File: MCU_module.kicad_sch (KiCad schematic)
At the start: 7 parts, among them U1 STM32C011F4U6TR, Y1 Crystal

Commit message: First basic design
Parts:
- removed C3, C4: CL, symbol Device:C_Small
- removed R1: R_Ref, symbol Device:R_Small
- removed U1: STM32C011F4U6TR, Package_DFN_QFN:ST_UFQFPN-20_3x3mm_P0.5mm, symbol MCU_ST_STM32C0:STM32C011F_4-6_Ux
- removed Y1: Crystal, symbol Device:Crystal_GND24
- added BOOT0: SW2, symbol Switch:SW_SPDT
- added C13: 4.7u, Capacitor_SMD:C_0402_1005Metric, symbol Device:C_Small
- added C14: 100n, Capacitor_SMD:C_0402_1005Metric, symbol Device:C_Small
- added C15: 1u, Capacitor_SMD:C_0402_1005Metric, symbol Device:C_Small
- added C16: 10n, Capacitor_SMD:C_0402_1005Metric, symbol Device:C_Small
- added C21: 0.1u, Capacitor_SMD:C_0402_1005Metric, symbol Device:C_Small
- added J2: SWD, Connector_PinHeader_1.27mm:PinHeader_2x05_P1.27mm_Vertical_SMD, symbol Connector_Generic:Conn_02x05_Odd_Even
- added R4: 10k, Resistor_SMD:R_0603_1608Metric, symbol Device:R_Small
- added SW1: NRST, symbol Switch:SW_SPST
- added U1: STM32F042G6U6, Package_DFN_QFN:QFN-28_4x4mm_P0.5mm, symbol MCU_ST_STM32F0:STM32F042G6Ux
- C1, C2: footprint (none) -> Capacitor_SMD:C_0402_1005Metric
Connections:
- net +3V3: now also BOOT0.3 (C), C13.1, C14.1, C15.1, C16.1, J2.1 (Pin_1), U1.17 (VDD), U1.18 (VDDIO2), U1.5 (VDDA)
- net GND: now also BOOT0.1 (A), C13.2, C14.2, C15.2, C16.2, C21.1, J2.3 (Pin_3), J2.5 (Pin_5), J2.9 (Pin_9), SW1.1 (A), U1.16 (VSSA)
- net SPI_CS: now also U1.23 (PA15)
- net SPI_MISO: now also U1.25 (PB4)
- net SPI_MOSI: now also U1.26 (PB5)
- net SPI_SCK: now also U1.24 (PB3)
- new net: BOOT0.2 (B), R4.1
- new net: R4.2, U1.1 (PB8)
- new net NRST: C21.2, J2.10 (Pin_10), SW1.2 (B), U1.4 (NRST)
- new net RF_CE: U1.27 (PB6)
- new net RF_IRQ: U1.28 (PB7)
- new net SWCLK: J2.4 (Pin_4), U1.22 (PA14)
- new net SWDIO: J2.2 (Pin_2), U1.21 (PA13)
- new net USB_D+: U1.20 (PA10/PA12)
- new net USB_D-: U1.19 (PA9/PA11)
- no-connect marks 0 -> 3

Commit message: Easier BOOT0
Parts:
- removed BOOT0: SW2, symbol Switch:SW_SPDT
- removed SW1: NRST, symbol Switch:SW_SPST
- added SW1: NRST, Button_Switch_SMD:SW_SPST_B3S-1000, symbol Switch:SW_Push
- added SW2: BOOT0, Button_Switch_SMD:SW_SPST_B3S-1000, symbol Switch:SW_Push
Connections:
- net +3V3: now also SW2.2
- net GND: now also R4.1, SW1.1
- net NRST: now also SW1.2
- net at R4.2, U1.1 (PB8): now also SW2.1
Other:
- moved on the sheet: R4

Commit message: Redesigned power supply. First board draft
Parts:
- SW1, SW2: footprint Button_Switch_SMD:SW_SPST_B3S-1000 -> Button_Switch_SMD:SW_SPST_B3U-1000P; JLCPCB C2733655 -> C231329
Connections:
- no-connect marks 3 -> 15
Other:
- moved on the sheet: C1, C13, C14, C15, C16, C2

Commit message: BOM assigned
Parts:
- C1, C13: LCSC (none) -> C82453
- C14, C2: LCSC (none) -> C1525
- C15: LCSC (none) -> C52923
- C16: LCSC (none) -> C15195
- C21: value 0.1u -> 100n; LCSC (none) -> C1525
- J2: LCSC (none) -> C4943297
- R4: LCSC (none) -> C25804
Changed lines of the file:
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@@
+			)
+		)
+		(property "LCSC" "C1525"
+			(at 181.61 31.75 0)
+			(effects
+				(font
+					(size 1.27 1.27)
+				)
+				(hide yes)
 			)
 		)
@@
 			)
 		)
+		(property "LCSC" "C4943297"
+			(at 113.03 43.18 0)
+			(effects
+				(font
+					(size 1.27 1.27)
+				)
+				(hide yes)
+			)
+		)
 		(pin "9"
 		)
@@
 			)
 		)
+		(property "LCSC" "C82453"
+			(at 172.72 31.75 0)
+			(effects
+				(font
+					(size 1.27 1.27)
+				)
+				(hide yes)
+			)
+		)
 		(pin "2"
 		)
@@
 			)
 		)
-		(property "Value" "0.1u"
+		(property "Value" "100n"
 			(at 156.2163 62.23 90)
 			(effects
@@
 			)
 		)
+		(property "LCSC" "C1525"
+			(at 156.21 66.04 90)
+			(effects
+				(font
+					(size 1.27 1.27)
+				)
+				(hide yes)
+			)
+		)
 		(pin "1"
 		)
@@
 			)
 		)
+		(property "LCSC" "C1525"
+			(at 163.83 31.75 0)
+			(effects
+				(font
+					(size 1.27 1.27)
+				)
+				(hide yes)
+			)
+		)
 		(pin "2"
 		)
@@
 			)
 		)
+		(property "LCSC" "C15195"
+			(at 199.39 31.75 0)
+			(effects
+				(font
+					(size 1.27 1.27)
+				)
+				(hide yes)
+			)
+		)
 		(pin "2"
 		)
@@
 			)
 		)
+		(property "LCSC" "C25804"
+			(at 142.24 109.22 0)
+			(effects
+				(font
+					(size 1.27 1.27)
+				)
+				(hide yes)
+			)
+		)
 		(pin "2"
 		)
@@
 			)
 		)
+		(property "LCSC" "C82453"
+			(at 154.94 31.75 0)
+			(effects
+				(font
+					(size 1.27 1.27)
+				)
+				(hide yes)
+			)
+		)
 		(pin "2"
 		)
@@
 			(at 190.5 31.75 0)
 			(effects
+				(font
+					(size 1.27 1.27)
+				)
+				(hide yes)
+			)
+		)
+		(property "LCSC" "C52923"
+			(at 190.5 31.75 0)
+			(effects

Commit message: Minor changes
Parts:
- C1, C13: LCSC C82453 -> (none); MPN (none) -> C82453
- C14, C2, C21: LCSC C1525 -> (none); MPN (none) -> C1525
- C15: LCSC C52923 -> (none); MPN (none) -> C52923
- C16: LCSC C15195 -> (none); MPN (none) -> C15195
- J2: footprint Connector_PinHeader_1.27mm:PinHeader_2x05_P1.27mm_Vertical_SMD -> Custom_Connectors:PinHeader_2x05_P1.27mm_Vertical_SMD_w_fiducials; JLCPCB Rotation Offset (none) -> -90; LCSC C4943297 -> (none); MPN (none) -> C4943297
- R4: LCSC C25804 -> (none); MPN (none) -> C25804
- SW1, SW2: JLCPCB C231329 -> (none); MPN (none) -> C231329
- U1: JLCPCB Rotation Offset (none) -> -90; LCSC C961597 -> (none); MPN (none) -> C961597
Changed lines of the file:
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@@
 			)
 		)
-		(property "LCSC" "C1525"
+		(property "MPN" "C1525"
 			(at 181.61 31.75 0)
 			(effects
@@
 			)
 		)
-		(property "Footprint" "Connector_PinHeader_1.27mm:PinHeader_2x05_P1.27mm_Vertical_SMD"
+		(property "Footprint" "Custom_Connectors:PinHeader_2x05_P1.27mm_Vertical_SMD_w_fiducials"
 			(at 113.03 43.18 0)
 			(effects
@@
 			)
 		)
-		(property "LCSC" "C4943297"
+		(property "MPN" "C4943297"
+			(at 113.03 43.18 0)
+			(effects
+				(font
+					(size 1.27 1.27)
+				)
+				(hide yes)
+			)
+		)
+		(property "JLCPCB Rotation Offset" "-90"
 			(at 113.03 43.18 0)
 			(effects
@@
 			)
 		)
-		(property "LCSC" "C82453"
+		(property "MPN" "C82453"
 			(at 172.72 31.75 0)
 			(effects
@@
 			)
 		)
-		(property "JLCPCB" "C231329"
+		(property "MPN" "C231329"
 			(at 156.21 55.88 0)
 			(effects
@@
 			)
 		)
-		(property "JLCPCB" "C231329"
+		(property "MPN" "C231329"
 			(at 142.24 97.79 0)
 			(effects
@@
 			)
 		)
-		(property "LCSC" "C961597"
+		(property "MPN" "C961597"
+			(at 186.69 91.44 0)
+			(effects
+				(font
+					(size 1.27 1.27)
+				)
+				(hide yes)
+			)
+		)
+		(property "JLCPCB Rotation Offset" "-90"
 			(at 186.69 91.44 0)
 			(effects
@@
 			)
 		)
-		(property "LCSC" "C1525"
+		(property "MPN" "C1525"
 			(at 156.21 66.04 90)
 			(effects
@@
 			)
 		)
-		(property "LCSC" "C1525"
+		(property "MPN" "C1525"
 			(at 163.83 31.75 0)
 			(effects
@@
 			)
 		)
-		(property "LCSC" "C15195"
+		(property "MPN" "C15195"
 			(at 199.39 31.75 0)
 			(effects
@@
 			)
 		)
-		(property "LCSC" "C25804"
+		(property "MPN" "C25804"
 			(at 142.24 109.22 0)
 			(effects
@@
 			)
 		)
-		(property "LCSC" "C82453"
+		(property "MPN" "C82453"
 			(at 154.94 31.75 0)
 			(effects
@@
 			)
 		)
-		(property "LCSC" "C52923"
+		(property "MPN" "C52923"
 			(at 190.5 31.75 0)
 			(effects

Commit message: Larger dimensions. Include mounting holes. Better antenna feed alignment
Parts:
- R4: footprint Resistor_SMD:R_0603_1608Metric -> Resistor_SMD:R_0402_1005Metric; MPN C25804 -> C25744
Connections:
- net GND: now also C21.2; no longer C21.1
- net NRST: now also C21.1; no longer C21.2
- net RF_CE: now also U1.8 (PA2); no longer U1.27 (PB6)
- net RF_IRQ: now also U1.2 (PF0); no longer U1.28 (PB7)
- net boot0: now reaches R4.2, SW2.1, U1.1 (PB8)
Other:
- moved on the sheet: C21
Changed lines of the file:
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@@
+	)
+	(no_connect
+		(at 171.45 99.06)
 	)
 	(no_connect
@@
 	)
 	(no_connect
-		(at 171.45 78.74)
+		(at 204.47 88.9)
 	)
 	(no_connect
-		(at 204.47 88.9)
-	)
-	(no_connect
-		(at 204.47 78.74)
+		(at 171.45 101.6)
 	)
 	(no_connect
@@
 	(wire
 		(pts
-			(xy 158.75 93.98) (xy 158.75 85.09)
+			(xy 148.59 93.98) (xy 148.59 85.09)
 		)
 		(stroke
@@
 	(wire
 		(pts
-			(xy 171.45 96.52) (xy 156.21 96.52)
+			(xy 171.45 96.52) (xy 146.05 96.52)
 		)
 		(stroke
@@
 	(wire
 		(pts
-			(xy 151.13 101.6) (xy 151.13 85.09)
-		)
-		(stroke
-			(width 0)
-			(type default)
-		)
-	)
-	(wire
-		(pts
 			(xy 163.83 34.29) (xy 163.83 36.83)
 		)
@@
 	(wire
 		(pts
-			(xy 171.45 101.6) (xy 151.13 101.6)
-		)
-		(stroke
-			(width 0)
-			(type default)
-		)
-	)
-	(wire
-		(pts
 			(xy 96.52 43.18) (xy 96.52 48.26)
 		)
@@
 	(wire
 		(pts
-			(xy 171.45 93.98) (xy 158.75 93.98)
+			(xy 171.45 93.98) (xy 148.59 93.98)
 		)
 		(stroke
@@
 	(wire
 		(pts
-			(xy 153.67 99.06) (xy 153.67 85.09)
-		)
-		(stroke
-			(width 0)
-			(type default)
-		)
-	)
-	(wire
-		(pts
 			(xy 163.83 36.83) (xy 154.94 36.83)
 		)
@@
 	(wire
 		(pts
-			(xy 156.21 96.52) (xy 156.21 85.09)
-		)
-		(stroke
-			(width 0)
-			(type default)
-		)
-	)
-	(wire
-		(pts
-			(xy 171.45 99.06) (xy 153.67 99.06)
+			(xy 146.05 96.52) (xy 146.05 85.09)
+		)
+		(stroke
+			(width 0)
+			(type default)
+		)
+	)
+	(wire
+		(pts
+			(xy 212.09 78.74) (xy 212.09 76.2)
 		)
 		(stroke
@@
 	(wire
 		(pts
-			(xy 161.29 91.44) (xy 161.29 85.09)
+			(xy 151.13 91.44) (xy 151.13 85.09)
 		)
 		(stroke
@@
 	(wire
 		(pts
+			(xy 165.1 78.74) (xy 171.45 78.74)
+		)
+		(stroke
+			(width 0)
+			(type default)
+		)
+	)
+	(wire
+		(pts
 			(xy 154.94 34.29) (xy 154.94 36.83)
 		)
@@
 	(wire
 		(pts
+			(xy 204.47 78.74) (xy 212.09 78.74)
+		)
+		(stroke
+			(width 0)
+			(type default)
+		)
+	)
+	(wire
+		(pts
 			(xy 171.45 73.66) (xy 163.83 73.66)
 		)
@@
 	(wire
 		(pts
-			(xy 171.45 91.44) (xy 161.29 91.44)
+			(xy 171.45 91.44) (xy 151.13 91.44)
 		)
 		(stroke
@@
 		)
 	)
-	(label "SWCLK"
-		(at 120.65 40.64 0)
+	(label "boot0"
+		(at 149.86 104.14 0)
 		(fields_autoplaced yes)
 		(effects
@@
 		)
 	)
-	(label "NRST"
-		(at 120.65 48.26 0)
+	(label "SWCLK"
+		(at 120.65 40.64 0)
 		(fields_autoplaced yes)
 		(effects
@@
 		)
 	)
-	(label "SWDIO"
-		(at 214.63 99.06 0)
+	(label "NRST"
+		(at 120.65 48.26 0)
 		(fields_autoplaced yes)
 		(effects
@@
 	)
 	(label "SWDIO"
-		(at 120.65 38.1 0)
+		(at 214.63 99.06 0)
 		(fields_autoplaced yes)
 		(effects
@@
 		)
 	)
-	(label "NRST"
-		(at 165.1 73.66 0)
+	(label "SWDIO"
+		(at 120.65 38.1 0)
 		(fields_autoplaced yes)
 		(effects
@@
 		)
 	)
-	(hierarchical_label "SPI_MOSI"
-		(shape input)
-		(at 156.21 85.09 90)
+	(label "NRST"
+		(at 165.1 73.66 0)
 		(fields_autoplaced yes)
 		(effects
@@
 				(size 1.27 1.27)
 			)
+			(justify left bottom)
+		)
+	)
+	(hierarchical_label "SPI_MOSI"
+		(shape input)
+		(at 146.05 85.09 90)
+		(fields_autoplaced yes)
+		(effects
+			(font
+				(size 1.27 1.27)
+			)
 			(justify left)
 		)
@@
 	(hierarchical_label "SPI_SCK"
 		(shape input)
-		(at 161.29 85.09 90)
+		(at 151.13 85.09 90)
 		(fields_autoplaced yes)
 		(effects
@@
 	(hierarchical_label "SPI_MISO"
 		(shape input)
-		(at 158.75 85.09 90)
+		(at 148.59 85.09 90)
 		(fields_autoplaced yes)
 		(effects
@@
 	(hierarchical_label "RF_IRQ"
 		(shape input)
-		(at 151.13 85.09 90)
+		(at 165.1 78.74 180)
 		(fields_autoplaced yes)
 		(effects
@@
 				(size 1.27 1.27)
 			)
-			(justify left)
+			(justify right)
 		)
 	)
 	(hierarchical_label "RF_CE"
 		(shape input)
-		(at 153.67 85.09 90)
+		(at 212.09 76.2 90)
 		(fields_autoplaced yes)
 		(effects
@@
 	(symbol
 		(lib_id "Device:C_Small")
-		(at 156.21 66.04 90)
+		(at 156.21 66.04 270)
+		(mirror x)
 		(unit 1)
 		(exclude_from_sim no)
@@
 		(on_board yes)
 		(dnp no)
-		(fields_autoplaced yes)
 		(property "Reference" "C21"
-			(at 156.2163 59.69 90)
+			(at 156.2037 59.69 90)
 			(effects
 				(font
@@
 		)
 		(property "Value" "100n"
-			(at 156.2163 62.23 90)
+			(at 156.2037 62.23 90)
 			(effects
 				(font
@@
 			)
 		)
-		(property "Footprint" "Resistor_SMD:R_0603_1608Metric"
+		(property "Footprint" "Resistor_SMD:R_0402_1005Metric"
 			(at 142.24 109.22 0)
 			(effects
@@
 			)
 		)
-		(property "MPN" "C25804"
+		(property "MPN" "C25744"
 			(at 142.24 109.22 0)
 			(effects

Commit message: Add signaling LEDs
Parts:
- added D301: SIG1, LED_SMD:LED_0603_1608Metric, symbol Device:LED_Small
- added D302: SIG2, LED_SMD:LED_0603_1608Metric, symbol Device:LED_Small
- added D303: SIG3, LED_SMD:LED_0603_1608Metric, symbol Device:LED_Small
- added D304: SIG4, LED_SMD:LED_0603_1608Metric, symbol Device:LED_Small
- added R301, R302, R303, R304: 2k2, Resistor_SMD:R_0402_1005Metric, symbol Device:R_Small
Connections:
- net GND: now also R301.2, R302.2, R303.2, R304.2
- net SIG3: now reaches U1.10 (PA4)
- net SIG3: now also D303.2 (A)
- net SIG2: now reaches U1.11 (PA5)
- net SIG2: now also D302.2 (A)
- net SIG1: now reaches U1.12 (PA6)
- net SIG1: now also D301.2 (A)
- net SIG4: now reaches U1.9 (PA3)
- net SIG4: now also D304.2 (A)
- new net: D304.1 (K), R304.1
- new net: D303.1 (K), R303.1
- new net: D301.1 (K), R301.1
- new net: D302.1 (K), R302.1
- no-connect marks 15 -> 11

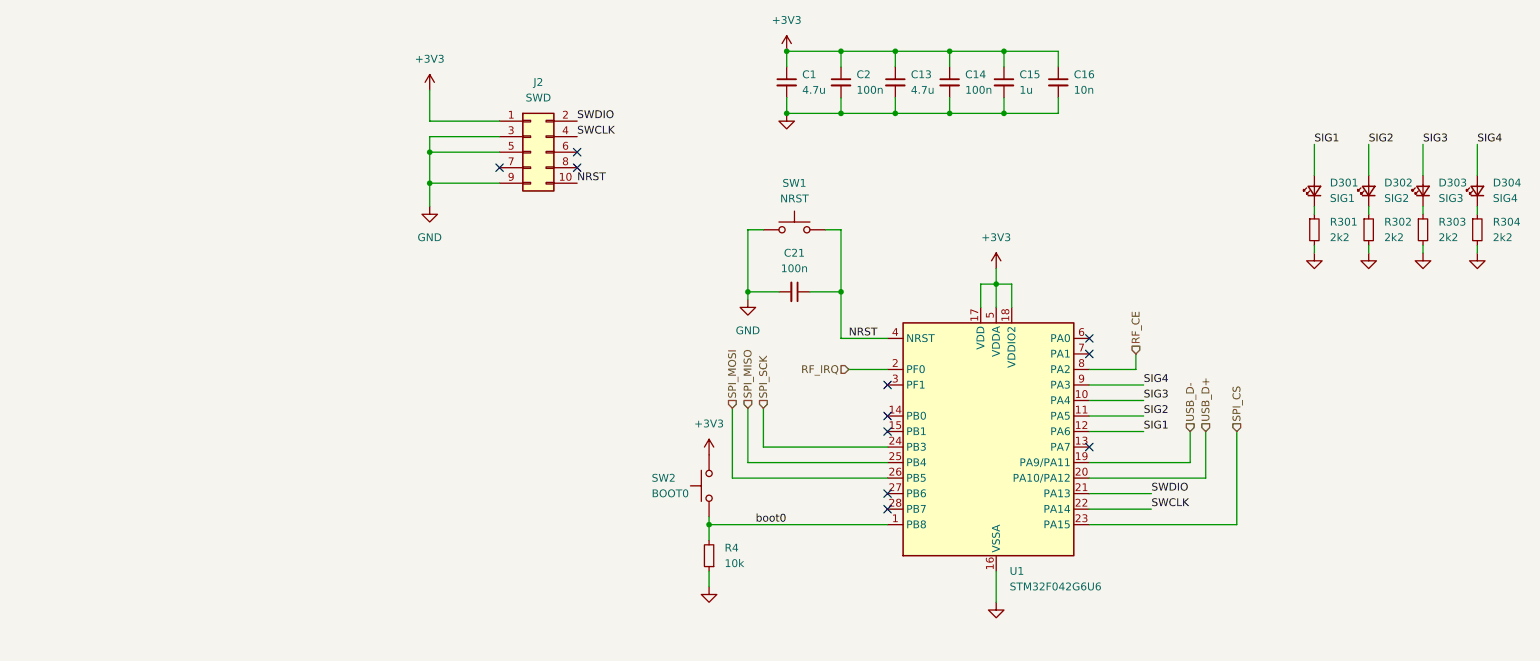
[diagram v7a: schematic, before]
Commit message: Migrated the STM32F0 to an STM32G0B
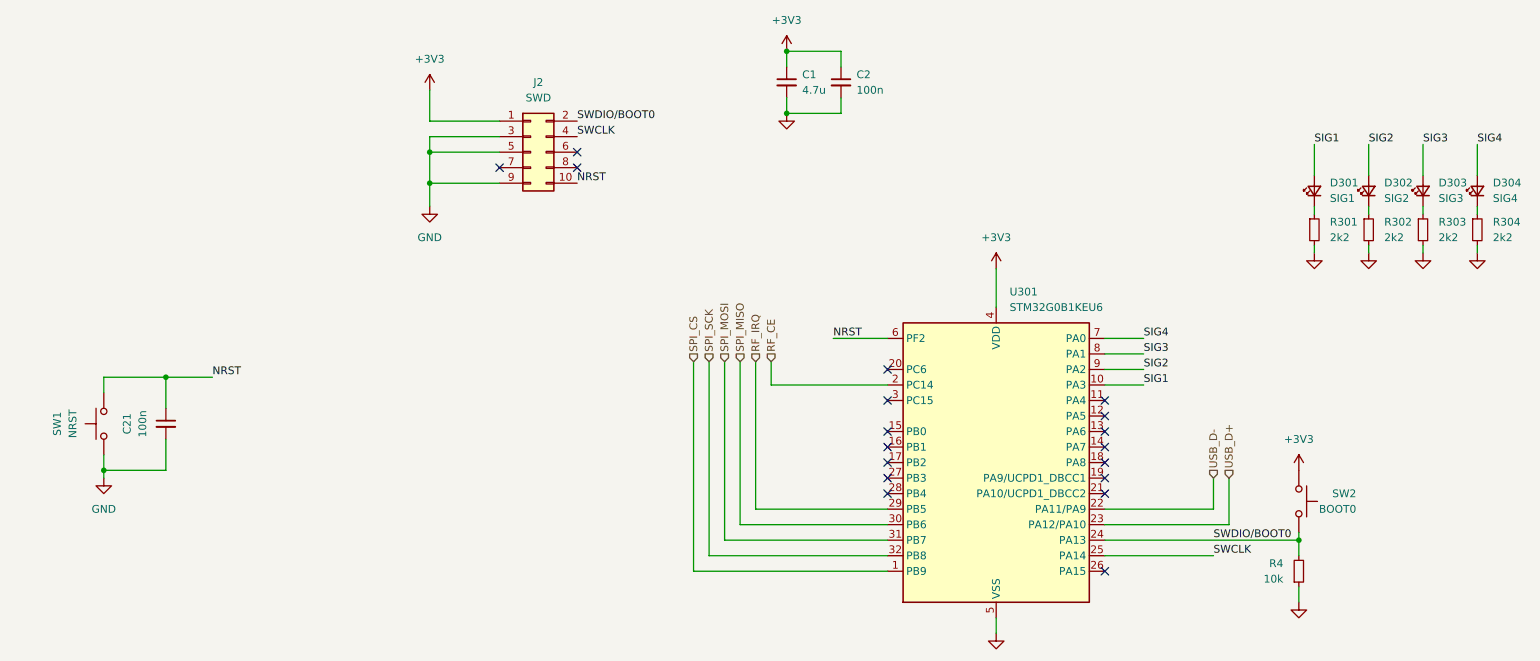
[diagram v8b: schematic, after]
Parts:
- removed C13: 4.7u, Capacitor_SMD:C_0402_1005Metric, symbol Device:C_Small
- removed C14: 100n, Capacitor_SMD:C_0402_1005Metric, symbol Device:C_Small
- removed C15: 1u, Capacitor_SMD:C_0402_1005Metric, symbol Device:C_Small
- removed C16: 10n, Capacitor_SMD:C_0402_1005Metric, symbol Device:C_Small
- removed U1: STM32F042G6U6, Package_DFN_QFN:QFN-28_4x4mm_P0.5mm, symbol MCU_ST_STM32F0:STM32F042G6Ux
- added U301: STM32G0B1KEU6, Package_DFN_QFN:QFN-32-1EP_5x5mm_P0.5mm_EP3.45x3.45mm, symbol MCU_ST_STM32G0:STM32G0B1KEUx
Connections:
- net boot0 is gone; now on net SWDIO/BOOT0: R4.2, SW2.1
- net +3V3: now also U301.4 (VDD)
- net GND: now also U301.33 (VSS), U301.5 (VSS)
- net NRST: now also U301.6 (PF2)
- net RF_CE: now also U301.2 (PC14)
- net RF_IRQ: now also U301.29 (PB5)
- net SIG1: now also U301.10 (PA3)
- net SIG2: now also U301.9 (PA2)
- net SIG3: now also U301.8 (PA1)
- net SIG4: now also U301.7 (PA0)
- net SPI_CS: now also U301.1 (PB9)
- net SPI_MISO: now also U301.30 (PB6)
- net SPI_MOSI: now also U301.31 (PB7)
- net SPI_SCK: now also U301.32 (PB8)
- net SWCLK: now also U301.25 (PA14)
- net USB_D+: now also U301.23 (PA12/PA10)
- net USB_D-: now also U301.22 (PA11/PA9)
- net SWDIO renamed SWDIO/BOOT0
- net SWDIO/BOOT0: now also U301.24 (PA13)
- no-connect marks 11 -> 18
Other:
- moved on the sheet: C21, R4, SW1, SW2
